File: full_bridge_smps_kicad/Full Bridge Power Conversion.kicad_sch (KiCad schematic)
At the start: 0 parts

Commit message: Adding the full bridge power conversion
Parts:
- added C18 (x13): 100n, symbol Device:C
- added C18: 1.5uF, symbol Device:C
- added C18 (x4): 22nF, symbol Device:C
- added D13, D14, D15, D8: BAT54S, fb_smps_footprints:BAT54S, symbol fb_smps_symbols:BAT54S
- added D5 (x2): DNP, symbol Device:D_Schottky
- added L3: 22uH, symbol Device:L
- added Q10, Q13, Q14, Q9: ~, fb_smps_footprints:PMD3001D, symbol fb_smps_symbols:PMD3001D
- added Q11, Q12, Q15 (x2): IRFB9N65A, fb_smps_footprints:IRFB9N65A, symbol fb_smps_symbols:IRFB9N65A
- added R53 (x4): 10.0, symbol Device:R_US
- added R53 (x4): DNP, symbol Device:R_US
- added R53 (x12): 100, symbol Device:R_US
- added R53: 3.3, symbol Device:R_US
- added T3, T6, T7: 450uH, fb_smps_footprints:P0584, symbol fb_smps_symbols:P0584
- added T4: P0584, fb_smps_footprints:P0584, symbol fb_smps_symbols:P0584
- added T5: ~, fb_smps_footprints:CS4100V-01L, symbol fb_smps_symbols:CS4100V-01L
- added T8: ~, symbol fb_smps_symbols:SP-RM_14
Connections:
- new net: Q11.1 (G), R53.1, R53.1
- new net: Q9.4 (N_E), Q9.4 (N_E), R53.2, R53.2, R53.2
- new net: C18.2, D5.1 (K), L3.2, Q11.2 (D), Q15.2 (D), R53.1
- new net: D8.1 (C2), D8.3 (AC), Q14.1 (B), Q14.1 (B), R53.1, T7.3
- new net: C18.2, C18.2, D8.2 (C2), Q14.2 (P_C), Q14.3 (P_C), T7.4, T7.8
- new net: Q14.4 (N_E), Q14.4 (N_E), R53.2, R53.2, R53.2
- new net: D15.1 (C2), D15.3 (AC), Q13.1 (B), Q13.1 (B), R53.1, T6.3
- new net: C18.2, C18.2, D15.2 (C2), Q13.2 (P_C), Q13.3 (P_C), T6.4, T6.8
- new net: C18.1, C18.2, C18.2, R53.2, T6.7
- new net: C18.2, C18.2, D13.2 (C2), Q9.2 (P_C), Q9.3 (P_C), T3.4, T3.8
- new net: D13.1 (C2), D13.3 (AC), Q9.1 (B), Q9.1 (B), R53.1, T3.3
- new net: C18.1, R53.1 (x8)
- new net: C18.1, C18.2, C18.2, R53.2, T3.7
- new net: C18.1, Q11.3 (S), Q12.2 (D)
- new net: T5.3, T8.1
- new net: C18.2, T8.2
- new net: C18.1, C18.2, C18.2, R53.2, T4.7
- new net: C18.1, D15.3 (AC), Q13.5 (N_C), Q13.6 (N_E), R53.2
- new net: Q15.1 (G), R53.1, R53.1 (x2)
- new net: D5.1 (K), D5.2 (A), Q15.2 (D), Q15.3 (S), T5.2
- new net: C18.1, C18.2, C18.2, R53.2, T7.7
- new net: C18.1, D13.3 (AC), Q9.5 (N_C), Q9.6 (N_E), R53.2
- new net: Q13.4 (N_E), Q13.4 (N_E), R53.2, R53.2, R53.2
- new net: D14.1 (C2), D14.3 (AC), Q10.1 (B), Q10.1 (B), R53.1, T4.3
- new net: C18.2, C18.2, D14.2 (C2), Q10.2 (P_C), Q10.3 (P_C), T4.4, T4.8
- new net: Q10.4 (N_E), Q10.4 (N_E), R53.2, R53.2, R53.2
- new net: Q12.1 (G), R53.1, R53.1
- new net: C18.1, D14.3 (AC), Q10.5 (N_C), Q10.6 (N_E), R53.2
- new net: C18.1, D8.3 (AC), Q14.5 (N_C), Q14.6 (N_E), R53.2
- new net +390V: L3.1, R53.2
- new net CURR_FB: T5.1
- new net DRV_A: T3.1
- new net DRV_B: T4.1
- new net DRV_C: T7.1
- new net DRV_D: T6.1
- new net GNDPWR: C18.1, D5.2 (A), Q12.3 (S), Q15.3 (S)
- new net GNDREF: T3.10, T4.10, T5.4, T6.10, T7.10
- new net SEC_+: T8.4
- new net SEC_REC_1: T8.3
- new net SEC_REC_2: T8.5
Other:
- note added: "FULL BRIDGE POWER CONVERSION"

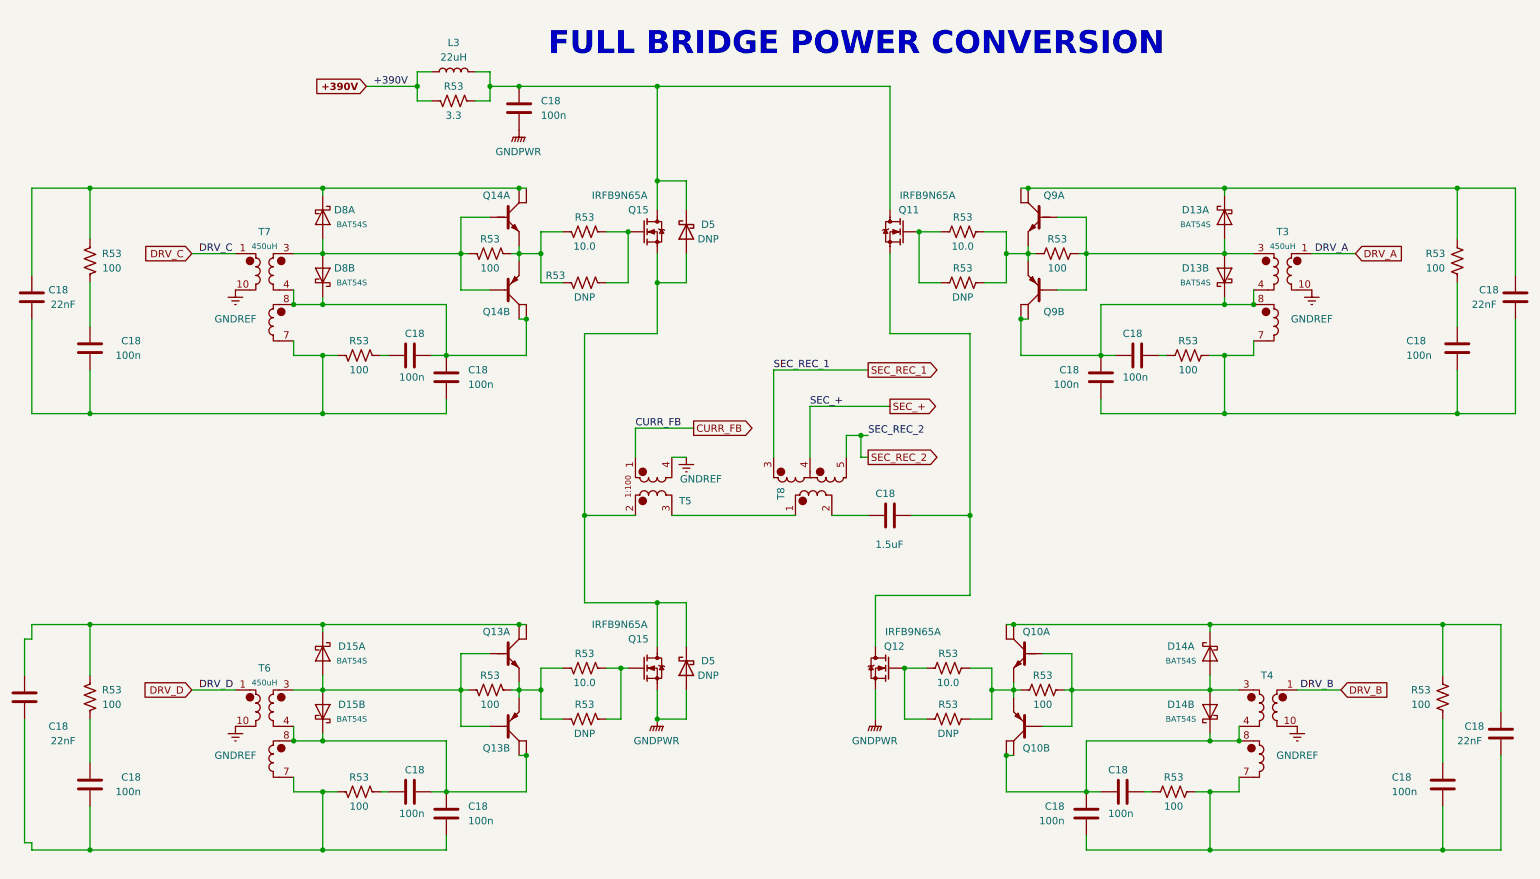
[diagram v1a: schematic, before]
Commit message: Finishing up the output rectification, creating new pages for the corresponding feedback and drive circuits
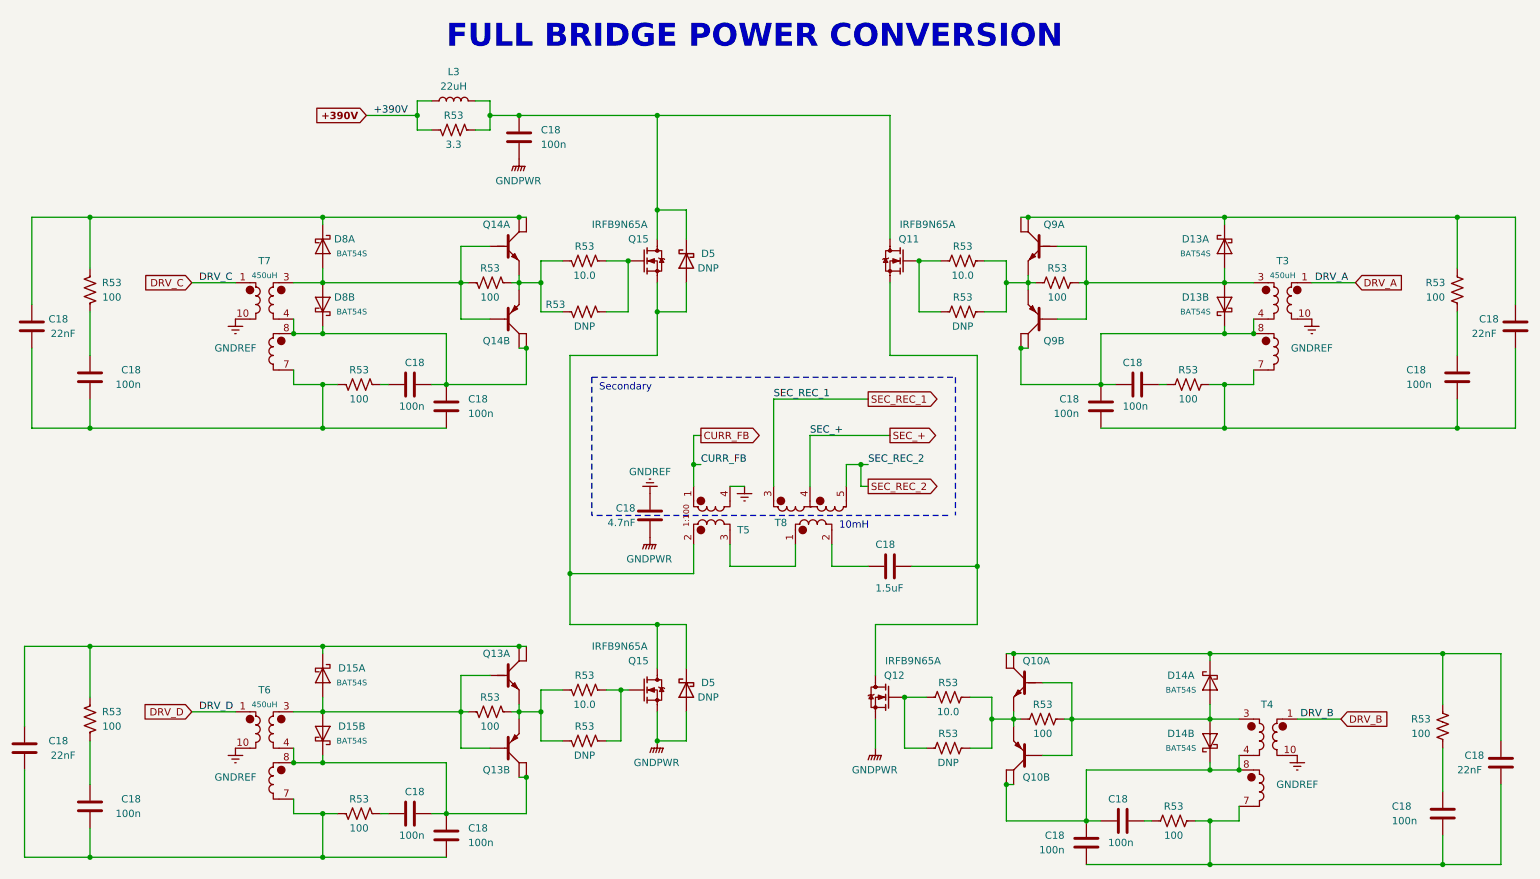
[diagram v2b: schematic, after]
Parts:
- added C18: 4.7nF, symbol Device:C
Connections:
- net GNDPWR: now also C18.2
- net GNDREF: now also C18.1
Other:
- note added: "10mH"
- note added: "Secondary"
- moved on the sheet: C18, D13A, D13B, D14A, D14B, D15A, D15B, D5, D8A, D8B, L3, Q10A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

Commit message: A bit of refactoring, saving work for the day
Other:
- note added: "A"
- note added: "B"
- note added: "C"
- note added: "D"
- note added: "Phase 1: A, D Phase 2: B, C"
- moved on the sheet: C18, D13A, D13B, D14A, D14B, D15A, D15B, D5, D8A, D8B, L3, Q10A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
